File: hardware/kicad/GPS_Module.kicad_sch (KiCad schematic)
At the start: 3 parts

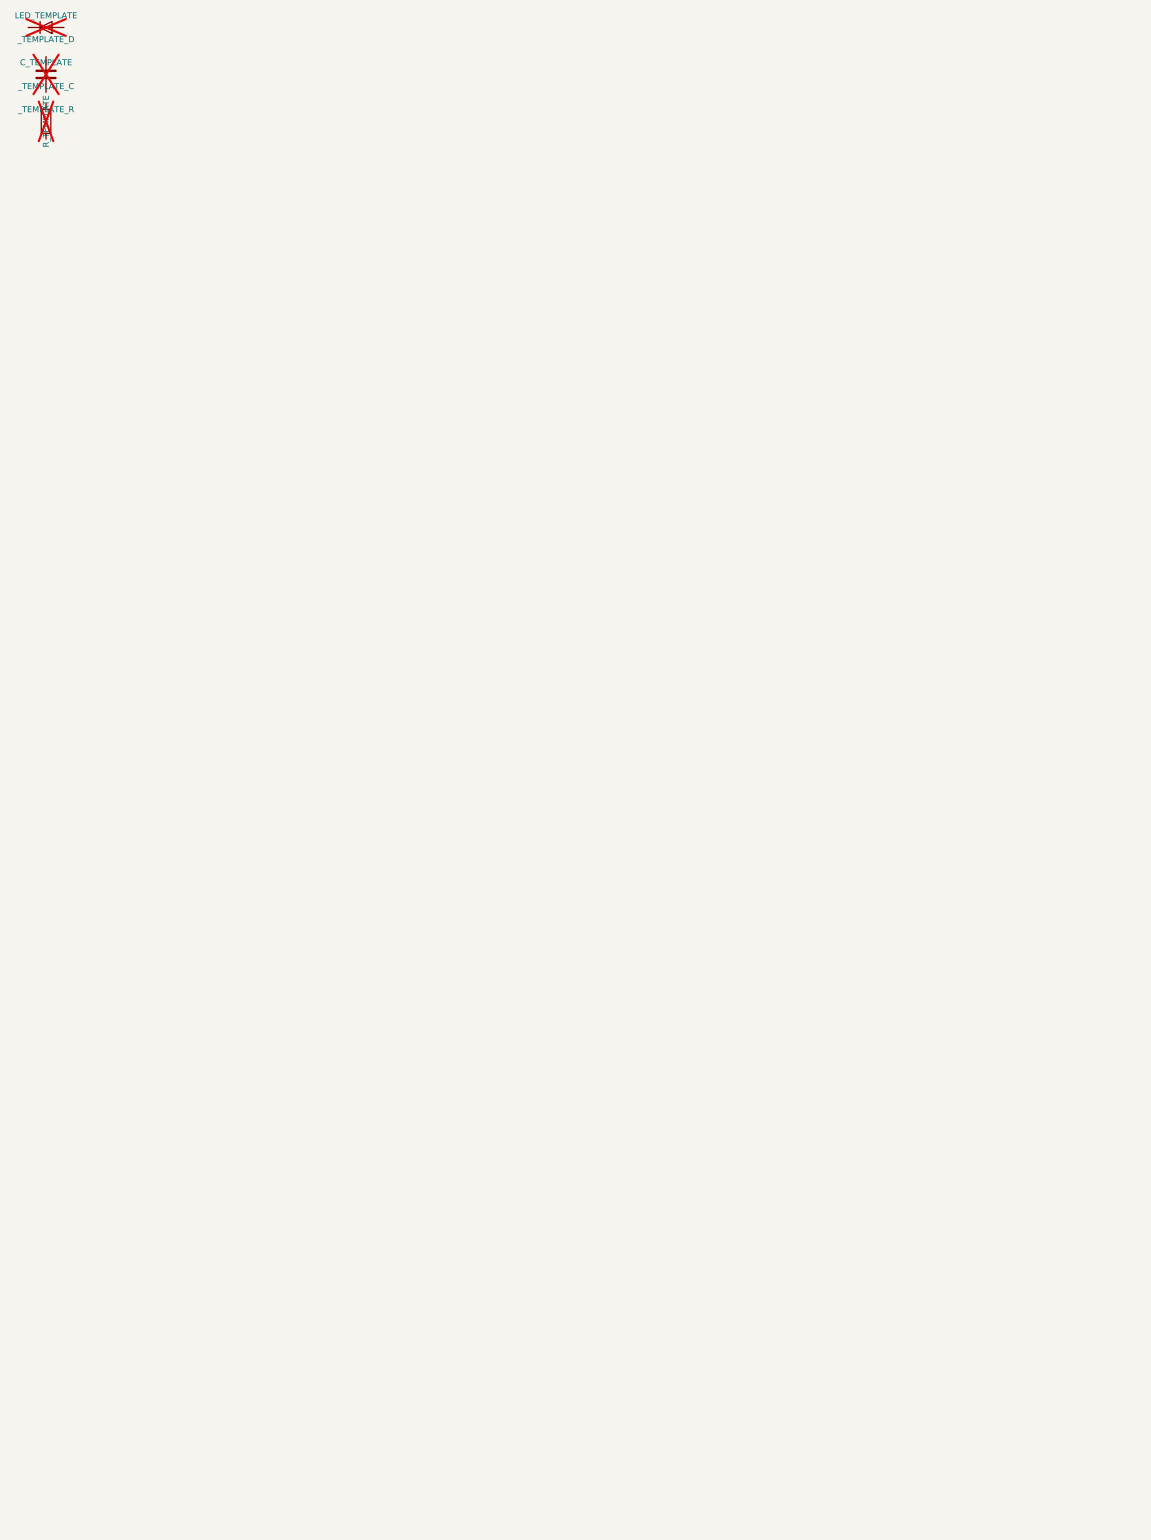
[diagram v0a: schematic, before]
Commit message: Phase A3: hierarchical V1 schematic generated from pstxnet.dat, ERC clean, netlist == pstxnet
gen_symbols.py (R1240N001x, TCAN1042H-Q1, CMS06 diode, VIN_RAW power symbol per current datasheets),
kicad_sym.py (flattened embedding of KiCad 9 library symbols), gen_sch.py (7 sub-sheets mirroring the OrCAD
blocks, labels/hierarchical pins/power symbols, deterministic symbol paths shared with the PCB via v1_design.py),
check_netlist.py (schematic and board nets == pstxnet.dat, refs and footprint paths match).
ERC 0 violations with --severity-all. Allegro refdes without a trailing digit get a '1' suffix (KiCad annotation
rule); original kept in the Allegro_RefDes property.

Co-Authored-By: Claude Fable 5.1 <noreply@anthropic.com>
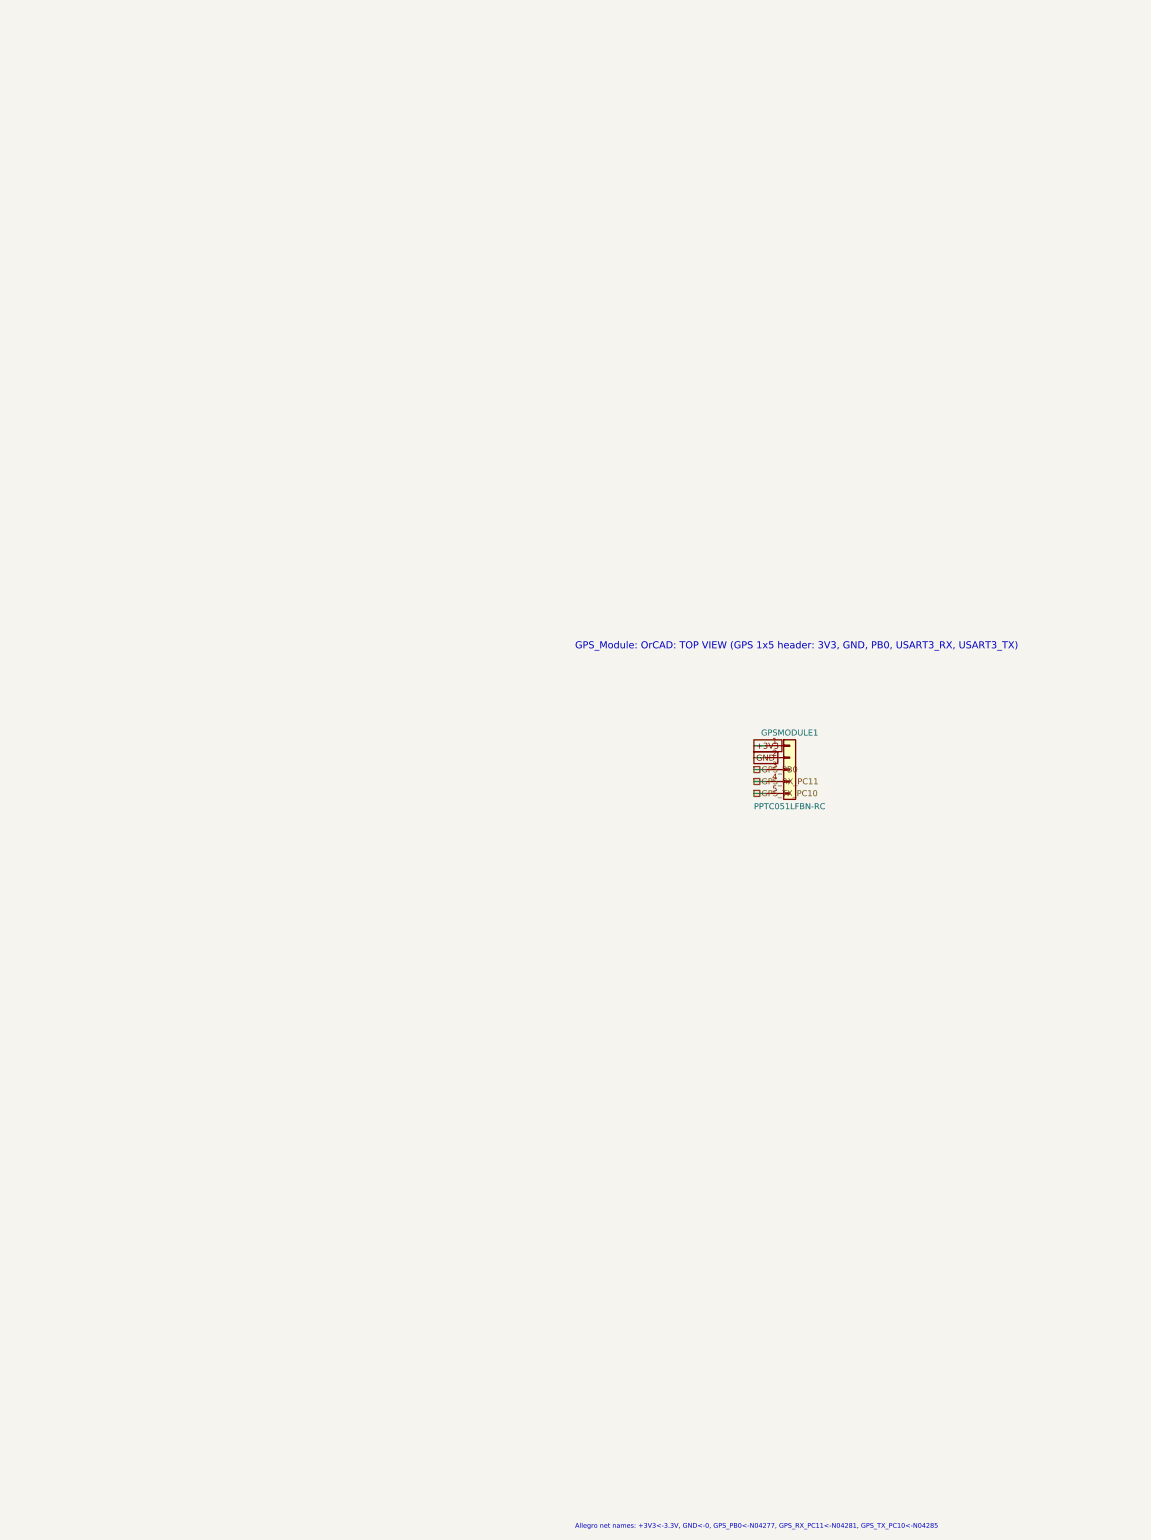
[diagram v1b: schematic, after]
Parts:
- removed _TEMPLATE_C: C_TEMPLATE, symbol Device:C
- removed _TEMPLATE_D: LED_TEMPLATE, symbol Device:LED
- removed _TEMPLATE_R: R_TEMPLATE, symbol Device:R
- added GPSMODULE1: PPTC051LFBN-RC, LoRa_Boat_Controller:CONN5_1LFBN-RC_SUL, symbol Connector_Generic:Conn_01x05
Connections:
- new net +3V3: GPSMODULE1.1 (Pin_1)
- new net GND: GPSMODULE1.2 (Pin_2)
- new net GPS_PB0: GPSMODULE1.3 (Pin_3)
- new net GPS_RX_PC11: GPSMODULE1.4 (Pin_4)
- new net GPS_TX_PC10: GPSMODULE1.5 (Pin_5)
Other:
- note added: "Allegro net names: +3V3<-3.3V, GND<-0, GPS_PB0<-N04277, GPS_RX_PC11<-N04281, GPS_TX_PC10<-N04285"
- note added: "GPS_Module: OrCAD: TOP VIEW (GPS 1x5 header: 3V3, GND, PB0, USART3_RX, USART3_TX)"
- company: (none) -> University of Arkansas EECS
- title: (none) -> LoRa Autonomous Boat Controller V1 - GPS_Module
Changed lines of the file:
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@@
+(kicad_sch
+	(version 20250114)
+	(generator "gen_sch.py")
+	(generator_version "9.0")
+	(paper "A4")
+	(title_block
+		(title "LoRa Autonomous Boat Controller V1 - GPS_Module")
+		(date "2025-05-09")
+		(rev "as fabricated (senior design v5.brd)")
+		(company "University of Arkansas EECS")
+		(comment 1 "OrCAD: TOP VIEW (GPS 1x5 header: 3V3, GND, PB0, USART3_RX, USART3_TX)")
+		(comment 2 "Generated by hardware/kicad/tools/gen_sch.py from pstxnet.dat (2025-05-09 17:12); see README.md")
+	)
+	(text "GPS_Module: OrCAD: TOP VIEW (GPS 1x5 header: 3V3, GND, PB0, USART3_RX, USART3_TX)"
+		(exclude_from_sim no)
+		(at 12.7 12.7 0)
+		(effects
+			(font
+				(size 1.5 1.5)
+			)
+			(justify left bottom)
+		)
+	)
+	(symbol
+		(lib_id "Connector_Generic:Conn_01x05")
+		(at 58.42 38.1 0)
+		(unit 1)
+		(exclude_from_sim no)
+		(in_bom yes)
+		(on_board yes)
+		(dnp no)
+		(property "Reference" "GPSMODULE1"
+			(at 58.42 30.25 0)
+			(effects
+				(font
+					(size 1.27 1.27)
+				)
+			)
+		)
+		(property "Value" "PPTC051LFBN-RC"
+			(at 58.42 45.95 0)
+			(effects
+				(font
+					(size 1.27 1.27)
+				)
+			)
+		)
+		(property "Footprint" "LoRa_Boat_Controller:CONN5_1LFBN-RC_SUL"
+			(at 58.42 38.1 0)
+			(effects
+				(font
+					(size 1.27 1.27)
+				)
+				(hide yes)
+			)
+		)
+		(property "Datasheet" "~"
+			(at 58.42 38.1 0)
+			(effects
+				(font
+					(size 1.27 1.27)
+				)
+				(hide yes)
+			)
+		)
+		(property "Description" "Generic connector, single row, 01x05, script generated (kicad-library-utils/schlib/autogen/connector/)"
+			(at 58.42 38.1 0)
+			(effects
+				(font
+					(size 1.27 1.27)
+				)
+				(hide yes)
+			)
+		)
+		(property "Allegro_Device" "PPTC051LFBN-RC_CONN5_1LFBN-RC_SUL_CONN5_1LFBN-RC"
+			(at 58.42 38.1 0)
+			(effects
+				(font
+					(size 1.27 1.27)
+				)
+				(hide yes)
+			)
+		)
+		(property "Allegro_RefDes" "GPSMODULE"
+			(at 58.42 38.1 0)
+			(effects
+				(font
+					(size 1.27 1.27)
+				)
+				(hide yes)
+			)
+		)
+		(pin "1"
+		)
+		(pin "2"
+		)
+		(pin "3"
+		)
+		(pin "4"
+		)
+		(pin "5"
+		)
+		(instances
+			(project "LoRa_Boat_Controller"
+				(path "/c954de34-2e36-5b27-b5cf-f634d7278a6a/9db88c42-176c-566e-9323-3aea3f09ec4b"
+					(reference "GPSMODULE1")
+					(unit 1)
+				)
+			)
+		)
+	)
+	(wire
+		(pts
+			(xy 53.34 33.02) (xy 50.8 33.02)
+		)
+		(stroke
+			(width 0)
+			(type default)
+		)
+	)
+	(global_label "+3V3"
+		(shape passive)
+		(at 50.8 33.02 180)
+		(effects
+			(font
+				(size 1.27 1.27)
+			)
+			(justify left bottom)
+		)
+	)
+	(wire
+		(pts
+			(xy 53.34 35.56) (xy 50.8 35.56)
+		)
+		(stroke
+			(width 0)
+			(type default)
+		)
+	)
+	(global_label "GND"
+		(shape passive)
+		(at 50.8 35.56 180)
+		(effects
+			(font
+				(size 1.27 1.27)
+			)
+			(justify left bottom)
+		)
+	)
+	(wire
+		(pts
+			(xy 53.34 38.1) (xy 50.8 38.1)
+		)
+		(stroke
+			(width 0)
+			(type default)
+		)
+	)
+	(hierarchical_label "GPS_PB0"
+		(shape passive)
+		(at 50.8 38.1 180)
+		(effects
+			(font
+				(size 1.27 1.27)
+			)
+			(justify left bottom)
+		)
+	)
+	(wire
+		(pts
+			(xy 53.34 40.64) (xy 50.8 40.64)
+		)
+		(stroke
+			(width 0)
+			(type default)
+		)
+	)
+	(hierarchical_label "GPS_RX_PC11"
+		(shape passive)
+		(at 50.8 40.64 180)
+		(effects
+			(font
+				(size 1.27 1.27)
+			)
+			(justify left bottom)
+		)
+	)
+	(wire
+		(pts
+			(xy 53.34 43.18) (xy 50.8 43.18)
+		)
+		(stroke
+			(width 0)
+			(type default)
+		)
+	)
+	(hierarchical_label "GPS_TX_PC10"
+		(shape passive)
+		(at 50.8 43.18 180)
+		(effects
+			(font
+				(size 1.27 1.27)
+			)
+			(justify left bottom)
+		)
+	)
+	(text "Allegro net names: +3V3<-3.3V, GND<-0, GPS_PB0<-N04277, GPS_RX_PC11<-N04281, GPS_TX_PC10<-N04285"
+		(exclude_from_sim no)
+		(at 12.7 200 0)
+		(effects
+			(font
+				(size 1.0 1.0)
+			)
+			(justify left bottom)
+		)
+	)
+	(embedded_fonts no)
+)

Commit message: Phase A3 close: CANH/CANL net names corrected, BOM with MPNs, DSN-v2 comparison, schematic exports
- gen_pcb.py: N04855 is CANL (U5 pin 6) and N24691 is CANH (U5 pin 7) per pstxnet.dat + TI SLLSES9D; the
  old NETLIST.md had them reversed (Codex review finding R03).
- gen_bom.py: docs/BOM.csv regenerated from the schematic with MPN/manufacturer/description/confidence/price
  columns (research in docs/research/BOM_MPN_RESEARCH.md, prices 2026-09-16).
- a0_xor_dsn.py: DSN v2 copper vs v5 films = 54 % / 63 % mismatch, 0 of 20 vias coincide, 0 of 45 parts unmoved;
  the DSN wiring is unusable for v5 (documented in docs/A0_PROVENANCE.md).
- Schematic PDF and per-sheet SVG exports in docs/img.
Gates: DRC 0 errors / 0 unconnected, ERC 0 violations, netlist check PASS, XOR F.Cu 0.87 % B.Cu 0.23 %.

Co-Authored-By: Claude Fable 5.1 <noreply@anthropic.com>
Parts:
- GPSMODULE1: MPN (none) -> PPTC051LFBN-RC; Manufacturer (none) -> Sullins Connector Solutions
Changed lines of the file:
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@@
 			)
 		)
-		(property "Description" "Generic connector, single row, 01x05, script generated (kicad-library-utils/schlib/autogen/connector/)"
+		(property "Description" "1x5 2.54 mm female header, through-hole"
 			(at 58.42 38.1 0)
 			(effects
@@
 			(at 58.42 38.1 0)
 			(effects
+				(font
+					(size 1.27 1.27)
+				)
+				(hide yes)
+			)
+		)
+		(property "MPN" "PPTC051LFBN-RC"
+			(at 58.42 38.1 0)
+			(effects
+				(font
+					(size 1.27 1.27)
+				)
+				(hide yes)
+			)
+		)
+		(property "Manufacturer" "Sullins Connector Solutions"
+			(at 58.42 38.1 0)
+			(effects
